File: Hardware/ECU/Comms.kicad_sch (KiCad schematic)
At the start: 10 parts, among them J1 Conn_01x04, U1 W25Q32JVSS, U2 MCP2562-E-SN, U3 74AHC1G32, U4 ADXL343

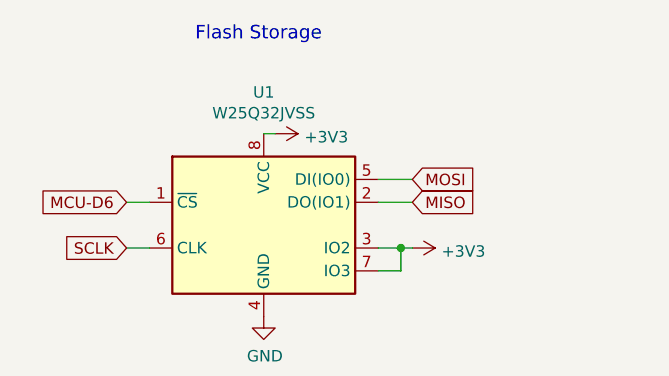
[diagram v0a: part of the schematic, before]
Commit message: modified:   .gitmodules 	modified:   Hardware/ECU/Comms.kicad_sch 	modified:   Hardware/ECU/ECU.kicad_pcb 	modified:   Hardware/ECU/ECU.kicad_pro 	modified:   Hardware/ECU/ECU.kicad_sch 	modified:   Hardware/ECU/Inputs.kicad_sch 	modified:   Hardware/ECU/Outputs.kicad_sch 	modified:   Hardware/ECU/fp-info-cache 	modified:   Hardware/ECU/fp-lib-table 	deleted:    docs/ECU info.url 	modified:   tune/Hayabusa-R1/CurrentTune.msq 	modified:   tune/Hayabusa-R1/projectCfg/project.properties 	modified:   tune/Hayabusa-R1/projectCfg/project.properties.bkup 	Hardware/ECU/ECU-backups/ECU-2024-11-07_084642.zip 	Hardware/ECU/ECU-backups/ECU-2024-11-07_091524.zip 	Hardware/ECU/ECU-backups/ECU-2024-11-07_094217.zip 	Hardware/ECU/ECU-backups/ECU-2024-11-07_120300.zip 	Hardware/ECU/ECU-backups/ECU-2024-11-08_085235.zip 	Hardware/ECU/ECU-backups/ECU-2024-11-08_091401.zip 	Hardware/ECU/ECU-backups/ECU-2024-11-08_103901.zip 	Hardware/ECU/docs/ 	Hardware/ECU/lib/2999/ 	Hardware/ECU/lib/IC_Automotive/IC_Automotive.pretty/BAT_2999.kicad_mod 	Hardware/ECU/lib/IC_Automotive/IC_Automotive.pretty/ZXMS6006DT8TA.kicad_mod 	Hardware/ECU/lib/ZXMS6006DT8TA/ 	Hardware/ECU/lib/teensy_library/ 	Hardware/ECU/output.pdf 	Hardware/ECU/report.txt 	docs/Speeduino_manual.pdf 	docs/Speeduino_manual.pdf:Zone.Identifier 	tune/Hayabusa-R1/dashboard/lambdaTable1Map.dash 	tune/Hayabusa-R1/dashboard/stagingMap.dash 	tune/TunerStudioAppDebug.txt
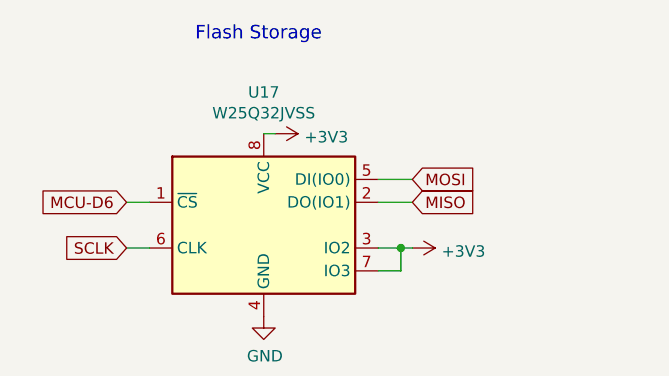
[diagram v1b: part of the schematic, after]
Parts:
- R1, R2: footprint Resistor_SMD:R_0805_2012Metric_Pad1.15x1.40mm_HandSolder -> Resistor_SMD:R_0805_2012Metric_Pad1.20x1.40mm_HandSolder
- renumbered U1 to U17
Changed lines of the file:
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@@
 			)
 		)
-		(property "Footprint" "Resistor_SMD:R_0805_2012Metric_Pad1.15x1.40mm_HandSolder"
+		(property "Footprint" "Resistor_SMD:R_0805_2012Metric_Pad1.20x1.40mm_HandSolder"
 			(at 97.028 144.78 90)
 			(effects
@@
 		(on_board yes)
 		(dnp no)
-		(property "Reference" "U1"
+		(property "Reference" "U17"
 			(at 62.23 51.2826 0)
 			(effects
@@
 			(project "ECU"
 				(path "/aaebd8f9-fdac-426b-87c0-a208167b6035/7d18358f-5866-4651-8656-b451f5c8ca1d"
-					(reference "U1")
+					(reference "U17")
 					(unit 1)
 				)
@@
 			)
 		)
-		(property "Footprint" "Resistor_SMD:R_0805_2012Metric_Pad1.15x1.40mm_HandSolder"
+		(property "Footprint" "Resistor_SMD:R_0805_2012Metric_Pad1.20x1.40mm_HandSolder"
 			(at 66.548 156.21 90)
 			(effects

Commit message: PCB
Platine Vernetzt
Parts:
- removed C1, C2: 0.1uF, Capacitor_SMD:C_0805_2012Metric, symbol Device:C
- removed JP1: Jumper_NO_Small, Jumper:SolderJumper-2_P1.3mm_Open_Pad1.0x1.5mm, symbol Device:Jumper_NO_Small
- removed R1: 0R, Resistor_SMD:R_0805_2012Metric_Pad1.20x1.40mm_HandSolder, symbol Device:R
- removed R2: 120R, Resistor_SMD:R_0805_2012Metric_Pad1.20x1.40mm_HandSolder, symbol Device:R
- removed U2: MCP2562-E-SN, Package_SO:SOIC-8_3.9x4.9mm_P1.27mm, symbol Interface_CAN_LIN:MCP2562-E-SN
- U17: footprint Package_SO:SOIC-8_5.23x5.23mm_P1.27mm -> Package_SO:SOIC-8_5.3x5.3mm_P1.27mm
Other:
- note removed: "CAN Transceiver"
- note removed: "Terminator resistor is optional and left off by default"
